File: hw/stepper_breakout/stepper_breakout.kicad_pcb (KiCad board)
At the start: 2 copper layers, 7 parts, among them J1 Conn_01x02_Pin, U1 Teensy4.1

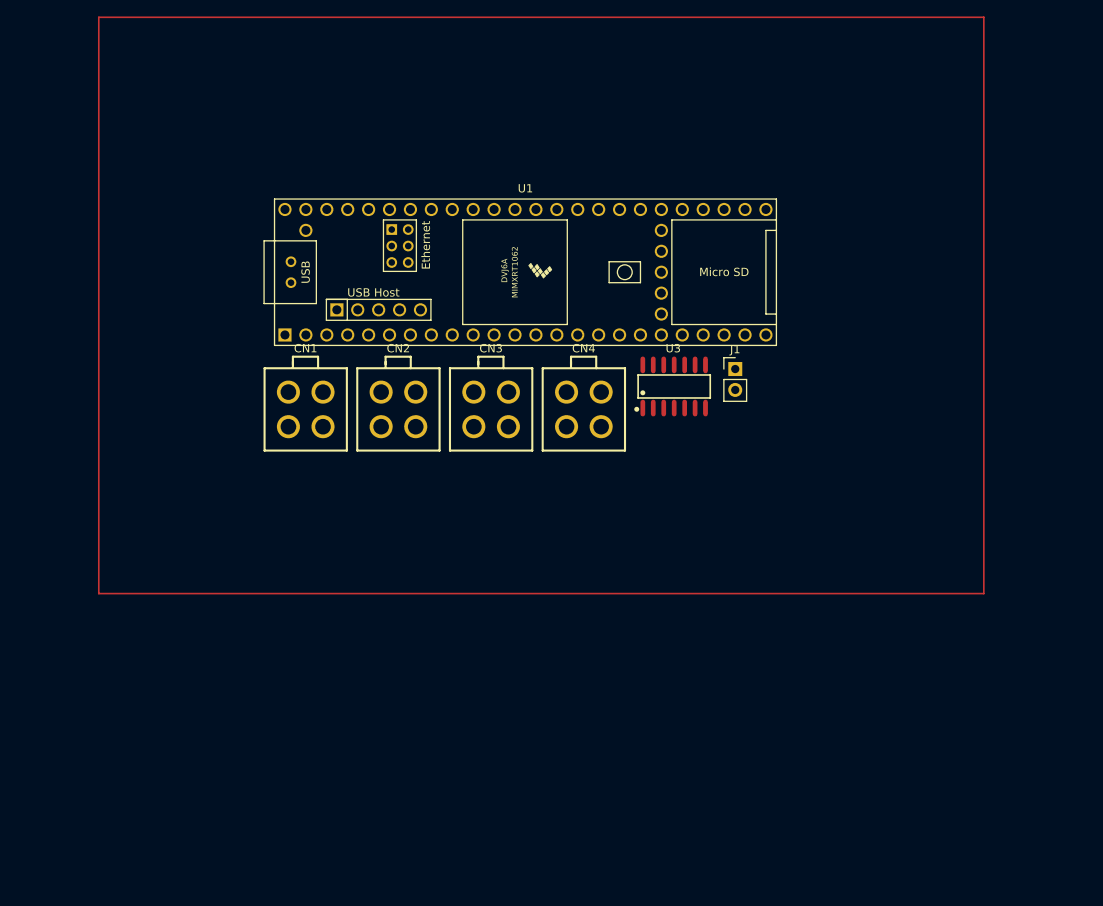
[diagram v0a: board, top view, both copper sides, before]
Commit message: Schematic + routing for teensy breakout
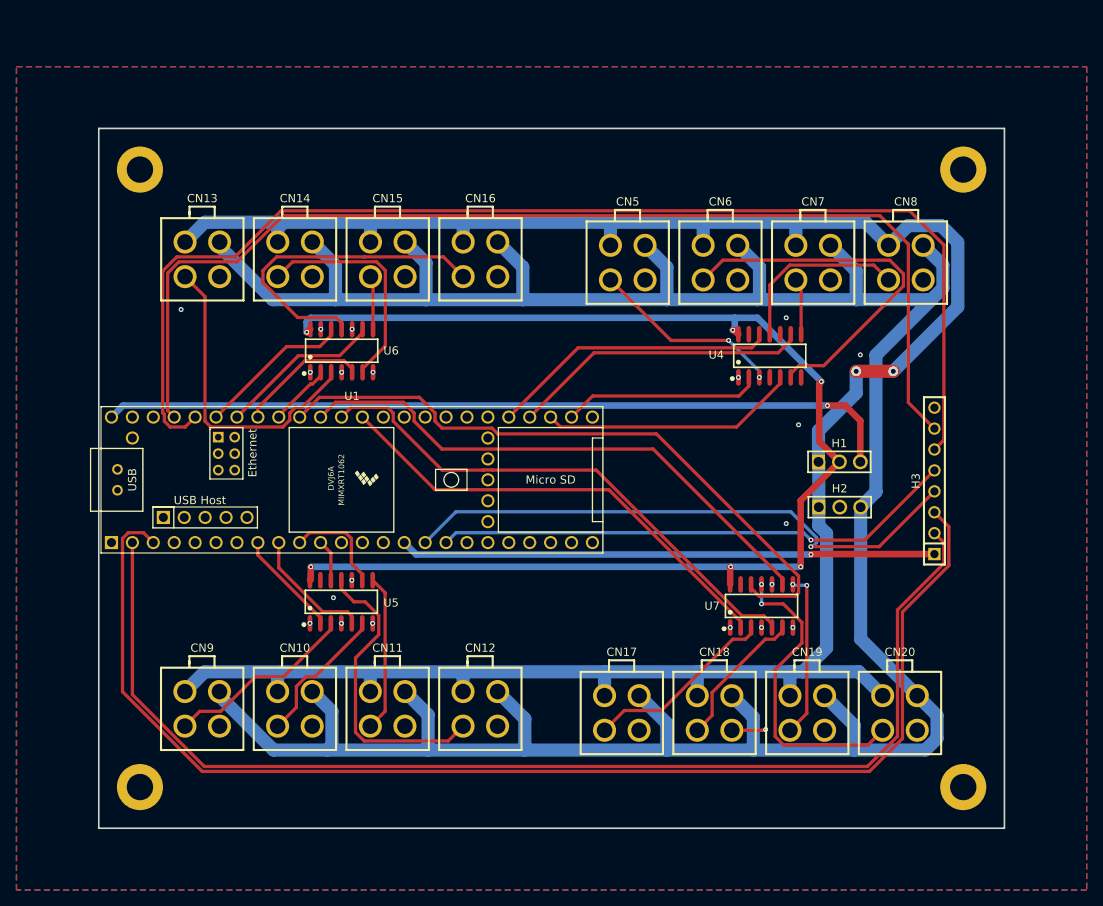
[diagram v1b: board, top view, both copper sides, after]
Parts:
- removed CN1, CN2, CN3, CN4: ~, EasyEDA_Lib:CONN-TH_HAA420A-4A
- removed J1: Conn_01x02_Pin, Connector_PinHeader_2.54mm:PinHeader_1x02_P2.54mm_Vertical
- removed U3: ~, EasyEDA_Lib:SOIC-14_L8.7-W3.9-P1.27-LS6.0-BL
- added CN10: ~, EasyEDA_Lib:CONN-TH_HAA420A-4A, F.Cu at (103.8, 128.0)
- added CN11: ~, EasyEDA_Lib:CONN-TH_HAA420A-4A, F.Cu at (115.1, 128.0)
- added CN12: ~, EasyEDA_Lib:CONN-TH_HAA420A-4A, F.Cu at (126.3, 128.0)
- added CN13: ~, EasyEDA_Lib:CONN-TH_HAA420A-4A, F.Cu at (92.6, 73.4)
- added CN14: ~, EasyEDA_Lib:CONN-TH_HAA420A-4A, F.Cu at (103.8, 73.4)
- added CN15: ~, EasyEDA_Lib:CONN-TH_HAA420A-4A, F.Cu at (115.1, 73.4)
- added CN16: ~, EasyEDA_Lib:CONN-TH_HAA420A-4A, F.Cu at (126.4, 73.4)
- added CN17: ~, EasyEDA_Lib:CONN-TH_HAA420A-4A, F.Cu at (143.5, 128.5)
- added CN18: ~, EasyEDA_Lib:CONN-TH_HAA420A-4A, F.Cu at (154.8, 128.5)
- added CN19: ~, EasyEDA_Lib:CONN-TH_HAA420A-4A, F.Cu at (166.1, 128.5)
- added CN20: ~, EasyEDA_Lib:CONN-TH_HAA420A-4A, F.Cu at (177.3, 128.5)
- added CN5: ~, EasyEDA_Lib:CONN-TH_HAA420A-4A, F.Cu at (144.2, 73.8)
- added CN6: ~, EasyEDA_Lib:CONN-TH_HAA420A-4A, F.Cu at (155.5, 73.8)
- added CN7: ~, EasyEDA_Lib:CONN-TH_HAA420A-4A, F.Cu at (166.8, 73.8)
- added CN8: ~, EasyEDA_Lib:CONN-TH_HAA420A-4A, F.Cu at (178.0, 73.8)
- added CN9: ~, EasyEDA_Lib:CONN-TH_HAA420A-4A, F.Cu at (92.6, 128.0)
- added H1: ~, EasyEDA_Lib:HDR-TH_3P-P2.54-V-M-1, F.Cu at (170.0, 98.0)
- added H2: ~, EasyEDA_Lib:HDR-TH_3P-P2.54-V-M-1, F.Cu at (170.0, 103.5)
- added H3: ~, EasyEDA_Lib:HDR-TH_8P-P2.54-V-M, F.Cu at (181.5, 100.3)
- added REF**: MountingHole_3.2mm_M3_DIN965_Pad, MountingHole:MountingHole_3.2mm_M3_DIN965_Pad, F.Cu at (85.0, 62.5)
- added REF**: MountingHole_3.2mm_M3_DIN965_Pad, MountingHole:MountingHole_3.2mm_M3_DIN965_Pad, F.Cu at (85.0, 137.5)
- added REF**: MountingHole_3.2mm_M3_DIN965_Pad, MountingHole:MountingHole_3.2mm_M3_DIN965_Pad, F.Cu at (185.0, 137.5)
- added REF**: MountingHole_3.2mm_M3_DIN965_Pad, MountingHole:MountingHole_3.2mm_M3_DIN965_Pad, F.Cu at (185.0, 62.5)
- added U4: ~, EasyEDA_Lib:SOIC-14_L8.7-W3.9-P1.27-LS6.0-BL, F.Cu at (161.5, 85.1)
- added U5: ~, EasyEDA_Lib:SOIC-14_L8.7-W3.9-P1.27-LS6.0-BL, F.Cu at (109.5, 115.0)
- added U6: ~, EasyEDA_Lib:SOIC-14_L8.7-W3.9-P1.27-LS6.0-BL, F.Cu at (109.5, 84.5)
- added U7: ~, EasyEDA_Lib:SOIC-14_L8.7-W3.9-P1.27-LS6.0-BL, F.Cu at (160.5, 115.5)
- moved U1 32.9 mm to (110.8, 100.2)
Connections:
- U1 pad 16: unconnected-(U1-24_A10_TX6_SCL2-Pad16) -> /SCL2
- U1 pad 17: unconnected-(U1-25_A11_RX6_SDA2-Pad17) -> /SDA2
- U1 pad 2: unconnected-(U1-0_RX1_CRX2_CS1-Pad2) -> /RX1
- U1 pad 3: unconnected-(U1-1_TX1_CTX2_MISO1-Pad3) -> /TX1
- U1 pad 36: unconnected-(U1-14_A0_TX3_SPDIF_OUT-Pad36) -> /STEP0B
- U1 pad 37: unconnected-(U1-15_A1_RX3_SPDIF_IN-Pad37) -> /STEP1B
- U1 pad 38: unconnected-(U1-16_A2_RX4_SCL1-Pad38) -> /STEP2B
- U1 pad 39: unconnected-(U1-17_A3_TX4_SDA1-Pad39) -> /STEP3B
- U1 pad 40: unconnected-(U1-18_A4_SDA-Pad40) -> /DIR0B
- U1 pad 41: unconnected-(U1-19_A5_SCL-Pad41) -> /DIR1B
- U1 pad 42: unconnected-(U1-20_A6_TX5_LRCLK1-Pad42) -> /DIR2B
- U1 pad 43: unconnected-(U1-21_A7_RX5_BCLK1-Pad43) -> /DIR3B
- U1 pad 44: unconnected-(U1-22_A8_CTX1-Pad44) -> /A8
- U1 pad 45: unconnected-(U1-23_A9_CRX1_MCLK1-Pad45) -> /A9
- U1 pad 48: +3V3 -> +5V
- U1 pad 49: +5V -> unconnected-(U1-VUSB-Pad49)
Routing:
- net SCGND: track 0.00 -> 346.2 mm
- net SC24V: track 0.00 -> 281.0 mm, vias 0 -> 2
- net V_lvl: track 0.00 -> 159.2 mm, vias 0 -> 6
- net /TX1: track 0.00 -> 154.1 mm
- net /A8: track 0.00 -> 147.8 mm
- net /RX1: track 0.00 -> 144.0 mm
- net /A9: track 0.00 -> 135.8 mm
- net +5V: track 0.00 -> 97.3 mm, vias 0 -> 1
- net /STEP3B: track 0.00 -> 80.0 mm
- net /SCL2: track 0.00 -> 69.7 mm, vias 0 -> 1
- net /STEP2B: track 0.00 -> 67.0 mm
- net +3V3: track 0.00 -> 65.0 mm, vias 0 -> 1
- net /STEP1B: track 0.00 -> 64.7 mm
- net /SDA2: track 0.00 -> 63.7 mm, vias 0 -> 1
- net /STEP0B: track 0.00 -> 57.0 mm
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- added copper zone on B.Cu, net GND
- added copper zone on F.Cu, net GND
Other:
- board outline added: 110 x 85 mm

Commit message: Fixed pcb connector pinout
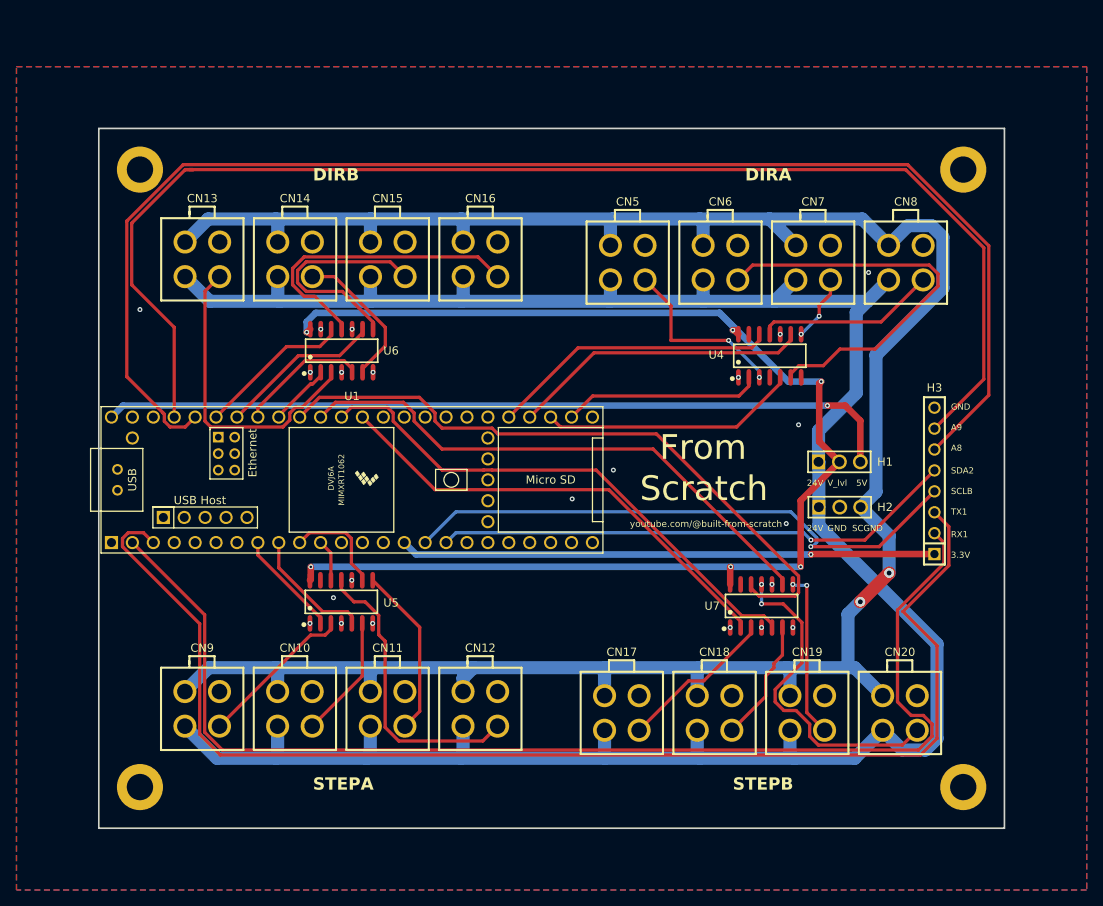
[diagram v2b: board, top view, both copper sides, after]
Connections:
- CN10 pad 1: /output1/OUT1 -> SC24V
- CN10 pad 2: SC24V -> SCGND
- CN10 pad 3: GND -> /output1/OUT1
- CN10 pad 4: SCGND -> GND
- CN11 pad 1: /output1/OUT2 -> SC24V
- CN11 pad 2: SC24V -> SCGND
- CN11 pad 3: GND -> /output1/OUT2
- CN11 pad 4: SCGND -> GND
- CN12 pad 1: /output1/OUT3 -> SC24V
- CN12 pad 2: SC24V -> SCGND
- CN12 pad 3: GND -> /output1/OUT3
- CN12 pad 4: SCGND -> GND
- CN13 pad 1: /output2/OUT0 -> SC24V
- CN13 pad 2: SC24V -> SCGND
- CN13 pad 3: GND -> /output2/OUT0
- CN13 pad 4: SCGND -> GND
- CN14 pad 1: /output2/OUT1 -> SC24V
- CN14 pad 2: SC24V -> SCGND
- CN14 pad 3: GND -> /output2/OUT1
- CN14 pad 4: SCGND -> GND
- CN15 pad 1: /output2/OUT2 -> SC24V
- CN15 pad 2: SC24V -> SCGND
- CN15 pad 3: GND -> /output2/OUT2
- CN15 pad 4: SCGND -> GND
- CN16 pad 1: /output2/OUT3 -> SC24V
- CN16 pad 2: SC24V -> SCGND
- CN16 pad 3: GND -> /output2/OUT3
- CN16 pad 4: SCGND -> GND
- CN17 pad 1: /output3/OUT0 -> SC24V
- CN17 pad 2: SC24V -> SCGND
- CN17 pad 3: GND -> /output3/OUT0
- CN17 pad 4: SCGND -> GND
- CN18 pad 1: /output3/OUT1 -> SC24V
- CN18 pad 2: SC24V -> SCGND
- CN18 pad 3: GND -> /output3/OUT1
- CN18 pad 4: SCGND -> GND
- CN19 pad 1: /output3/OUT2 -> SC24V
- CN19 pad 2: SC24V -> SCGND
- CN19 pad 3: GND -> /output3/OUT2
- CN19 pad 4: SCGND -> GND
- CN20 pad 1: /output3/OUT3 -> SC24V
- CN20 pad 2: SC24V -> SCGND
- CN20 pad 3: GND -> /output3/OUT3
- CN20 pad 4: SCGND -> GND
- CN5 pad 1: /output/OUT0 -> SC24V
- CN5 pad 2: SC24V -> SCGND
- CN5 pad 3: GND -> /output/OUT0
- CN5 pad 4: SCGND -> GND
- CN6 pad 1: /output/OUT1 -> SC24V
- CN6 pad 2: SC24V -> SCGND
- CN6 pad 3: GND -> /output/OUT1
- CN6 pad 4: SCGND -> GND
- CN7 pad 1: /output/OUT2 -> SC24V
- CN7 pad 2: SC24V -> SCGND
- CN7 pad 3: GND -> /output/OUT2
- CN7 pad 4: SCGND -> GND
- CN8 pad 1: /output/OUT3 -> SC24V
- CN8 pad 2: SC24V -> SCGND
- CN8 pad 3: GND -> /output/OUT3
- CN8 pad 4: SCGND -> GND
- CN9 pad 1: /output1/OUT0 -> SC24V
- CN9 pad 2: SC24V -> SCGND
- CN9 pad 3: GND -> /output1/OUT0
- CN9 pad 4: SCGND -> GND
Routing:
- net SCGND: track 346.2 -> 283.3 mm, vias 0 -> 2
- net /A9: track 135.8 -> 161.8 mm
- net /A8: track 147.8 -> 169.9 mm
- net /output2/OUT2: track 6.51 -> 27.7 mm
- net /output2/OUT1: track 27.8 -> 18.0 mm
- net SC24V: track 281.0 -> 286.1 mm, vias 2 -> 0
- net /output1/OUT0: track 23.3 -> 19.1 mm
- net /output3/OUT0: track 23.4 -> 19.2 mm
- net GND: track 4.15 -> 0.00 mm, vias 21 -> 22
- net /output/OUT1: track 46.0 -> 49.7 mm
- net /output2/OUT3: track 39.8 -> 37.1 mm
- net /RX1: track 144.0 -> 146.7 mm
- net /output3/OUT3: track 37.6 -> 40.2 mm
- net /output3/OUT1: track 17.4 -> 15.0 mm
- net /output1/OUT1: track 17.4 -> 15.0 mm
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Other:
- board text added: "24V"
- board text added: "3.3V"
- board text added: "5V"
- board text added: "A8"
- board text added: "A9"
- board text added: "DIRA"
- board text added: "DIRB"
- board text added: "From"
- board text added: "GND"
- board text added: "RX1"
- board text added: "SCGND"
- board text added: "SCLB"
- board text added: "SDA2"
- board text added: "STEPA"
- board text added: "STEPB"
- board text added: "Scratch"
- board text added: "TX1"
- board text added: "V_lvl"
- board text added: "youtube.com/@built-from-scratch"

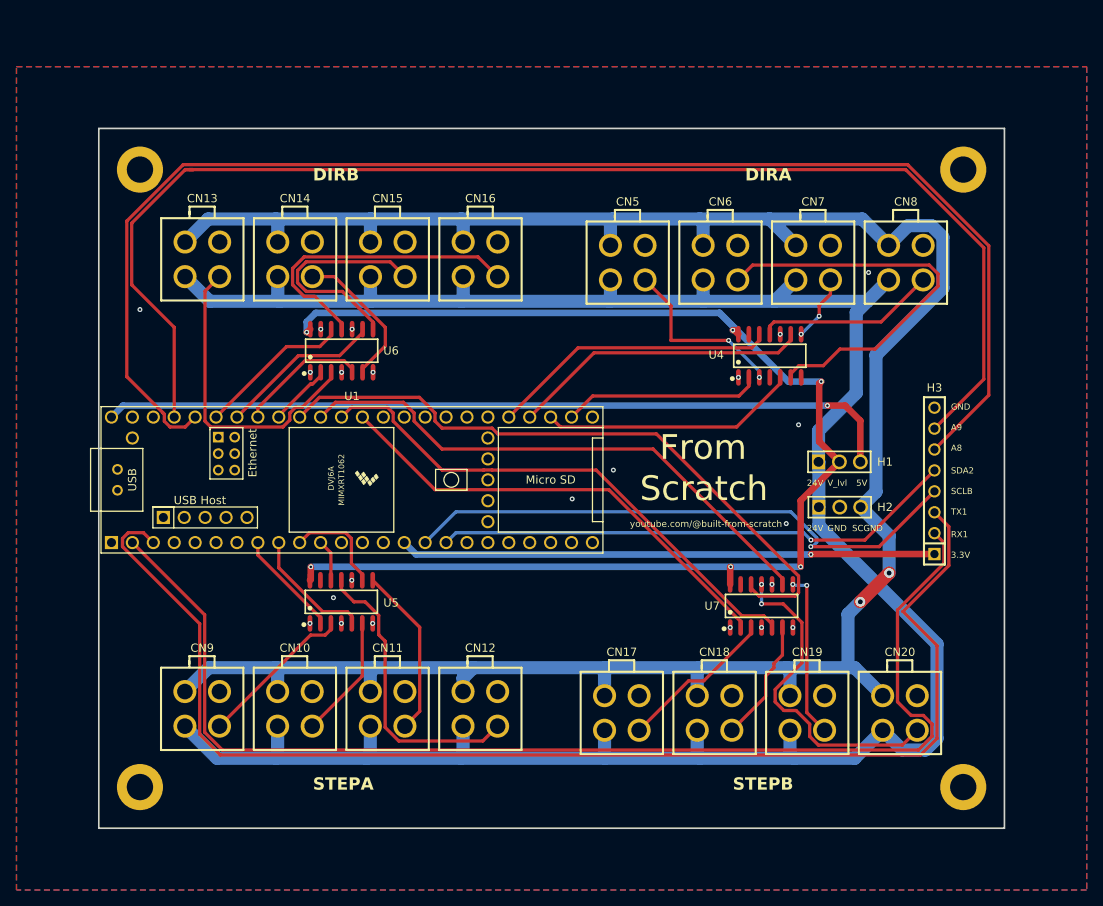
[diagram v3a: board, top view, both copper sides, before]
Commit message: Added test mode
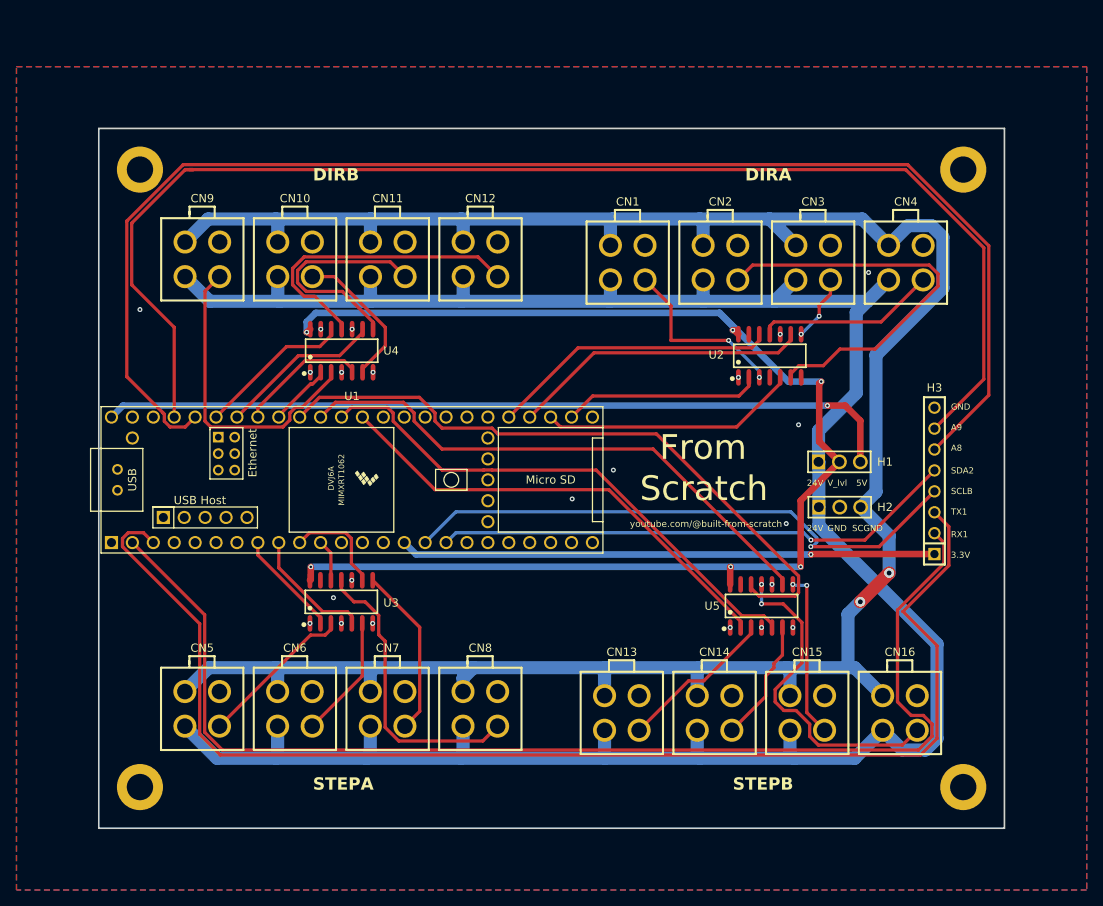
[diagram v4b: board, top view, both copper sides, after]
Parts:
- renumbered CN5 to CN1, CN14 to CN10, CN15 to CN11, CN16 to CN12, CN17 to CN13, CN18 to CN14, CN19 to CN15, CN20 to CN16, CN6 to CN2, CN7 to CN3, CN8 to CN4, CN9 to CN5, CN10 to CN6, CN11 to CN7, CN12 to CN8, CN13 to CN9, U4 to U2, U5 to U3, U6 to U4, U7 to U5
